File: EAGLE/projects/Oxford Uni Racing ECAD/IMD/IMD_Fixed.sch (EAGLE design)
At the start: 13 parts, among them IC1 LM2901N, IC2 555, J2 T821108A1S100CEU, K1 RT444012, X1 Connector i

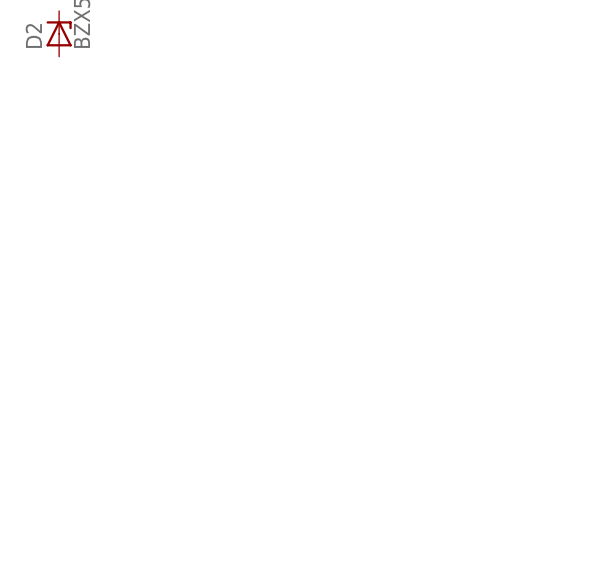
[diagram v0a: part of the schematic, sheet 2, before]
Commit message: added decoupling capacitors
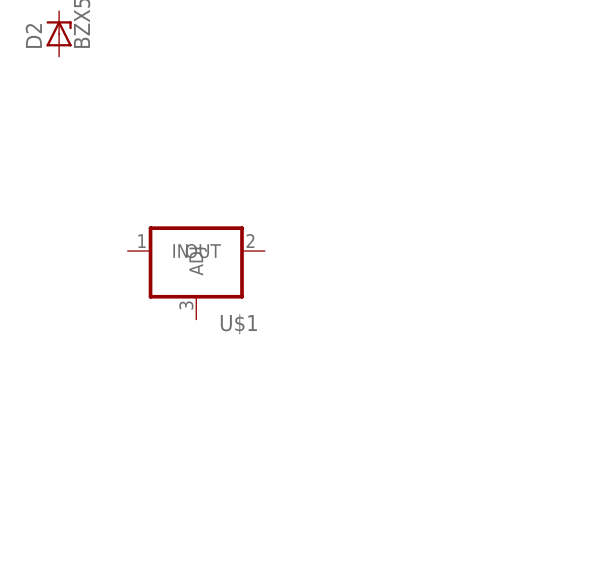
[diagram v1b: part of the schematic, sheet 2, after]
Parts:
- added U$1: (no value), v-reg_supertex:N3
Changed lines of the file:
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@@
 <part name="IC2" library="SparkFun-IC-Special-Function" library_urn="urn:adsk.eagle:library:527" deviceset="555" device="KIT" package3d_urn="urn:adsk.eagle:package:39188/1" value="555"/>
 <part name="OK1" library="optocoupler" library_urn="urn:adsk.eagle:library:320" deviceset="6N135" device="" package3d_urn="urn:adsk.eagle:package:21941/1"/>
+<part name="U$1" library="v-reg_supertex" deviceset="N3" device=""/>
 </parts>
 <sheets>
@@
 <attribute name="VALUE" x="36.195" y="-43.18" size="1.778" layer="96"/>
 </instance>
+<instance part="U$1" gate="G$1" x="45.72" y="15.24" smashed="yes">
+<attribute name="NAME" x="48.26" y="7.62" size="1.778" layer="95"/>
+<attribute name="VALUE" x="48.26" y="5.08" size="1.778" layer="96"/>
+</instance>
 </instances>
